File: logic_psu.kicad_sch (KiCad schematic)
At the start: 68 parts, among them Q13 BSS138, Q14 UMH3N, Q15 IPD50R3K0CE, Q16 BSS138, Q17 BSS138, Q18 BSS138, Q19 BSS138, SW1 EG1224, T1 DA2032-ALD, U3 LM1117MP-3.3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

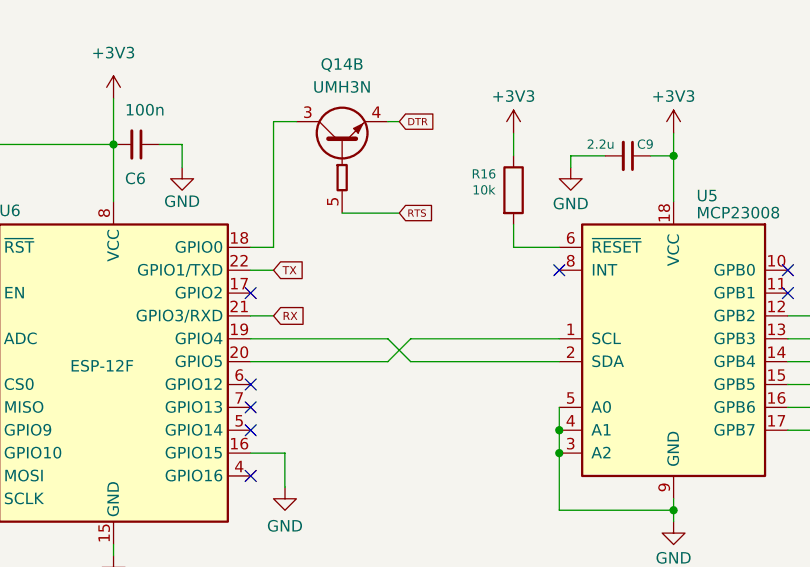
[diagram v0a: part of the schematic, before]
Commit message: fixed pull-ups
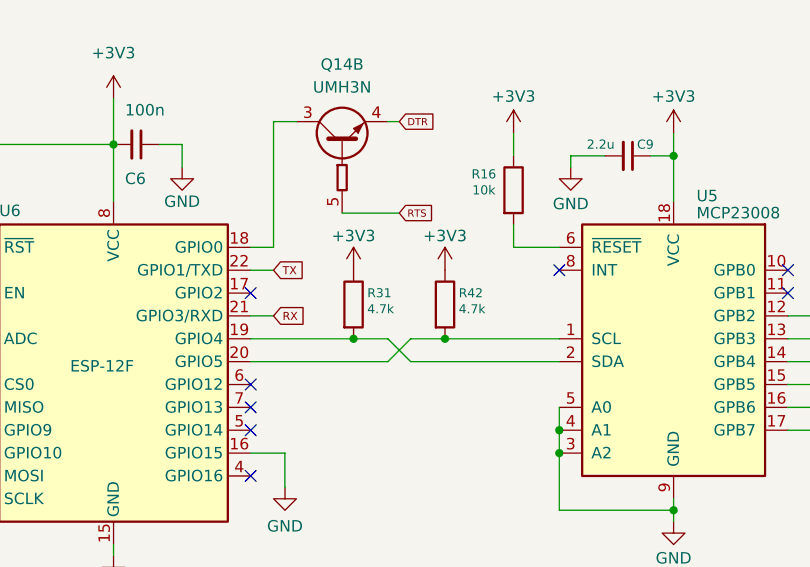
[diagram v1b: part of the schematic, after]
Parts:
- added R31, R42: 4.7k, Resistor_SMD:R_0603_1608Metric, symbol Device:R
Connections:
- net +3V3: now also R31.1, R42.1
- net at U5.2 (SDA), U6.19 (GPIO4): now also R31.2
- net at U5.1 (SCL), U6.20 (GPIO5): now also R42.2

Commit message: updated lcsc parts
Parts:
- C12, C13, C9: LCSC Part Number (none) -> C19110
- C14: LCSC Part Number (none) -> C5674
- C15, C16, C17, C18: LCSC Part Number (none) -> C5189825
- C19, C28, C29: LCSC Part Number (none) -> C85713
- C20, C3, C4, C6: LCSC Part Number (none) -> C14663
- C21: LCSC Part Number (none) -> C1853160
- C22: LCSC Part Number (none) -> C5128373
- C23: LCSC Part Number (none) -> C519405
- C24, C25: LCSC Part Number (none) -> C377089
- C5: LCSC Part Number (none) -> C165101
- D1: LCSC Part Number (none) -> C364563
- D2: LCSC Part Number (none) -> C2981449
- D3: LCSC Part Number (none) -> C2827688
- D4: LCSC Part Number (none) -> C707998
- D5: LCSC Part Number (none) -> C962640
- F1: LCSC Part Number (none) -> C2649922
- Q13, Q16, Q17, Q18, Q19: LCSC Part Number (none) -> C5224260
- Q14: LCSC Part Number (none) -> C123008
- Q15: LCSC Part Number (none) -> C536788
- R14, R15: LCSC Part Number (none) -> C253328
- R16, R17, R18, R19, R22, R25, R30, R32, R33, R34, R35, R36, R37, R38, R39: LCSC Part Number (none) -> C510087
- R20, R21: LCSC Part Number (none) -> C2091513
- R23, R24: LCSC Part Number (none) -> C22875
- R26: LCSC Part Number (none) -> C873681
- R27: LCSC Part Number (none) -> C164156
- R28: LCSC Part Number (none) -> C17927
- R29: LCSC Part Number (none) -> C23093
- R31, R42: LCSC Part Number (none) -> C99782
- SW1: LCSC Part Number (none) -> C273395
- T1: LCSC Part Number (none) -> C7938441
- U3: LCSC Part Number (none) -> C498153
- U4: LCSC Part Number (none) -> C5246810
- U5: LCSC Part Number (none) -> C92253
- U6: LCSC Part Number (none) -> C19949064
- U7: LCSC Part Number (none) -> C580135
- U8: LCSC Part Number (none) -> C179599
- USB1: LCSC Part Number (none) -> C3020560
